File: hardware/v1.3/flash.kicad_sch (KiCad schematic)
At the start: 10 parts, among them U1 ECP5-CABGA256, U11 W25Q128JVS

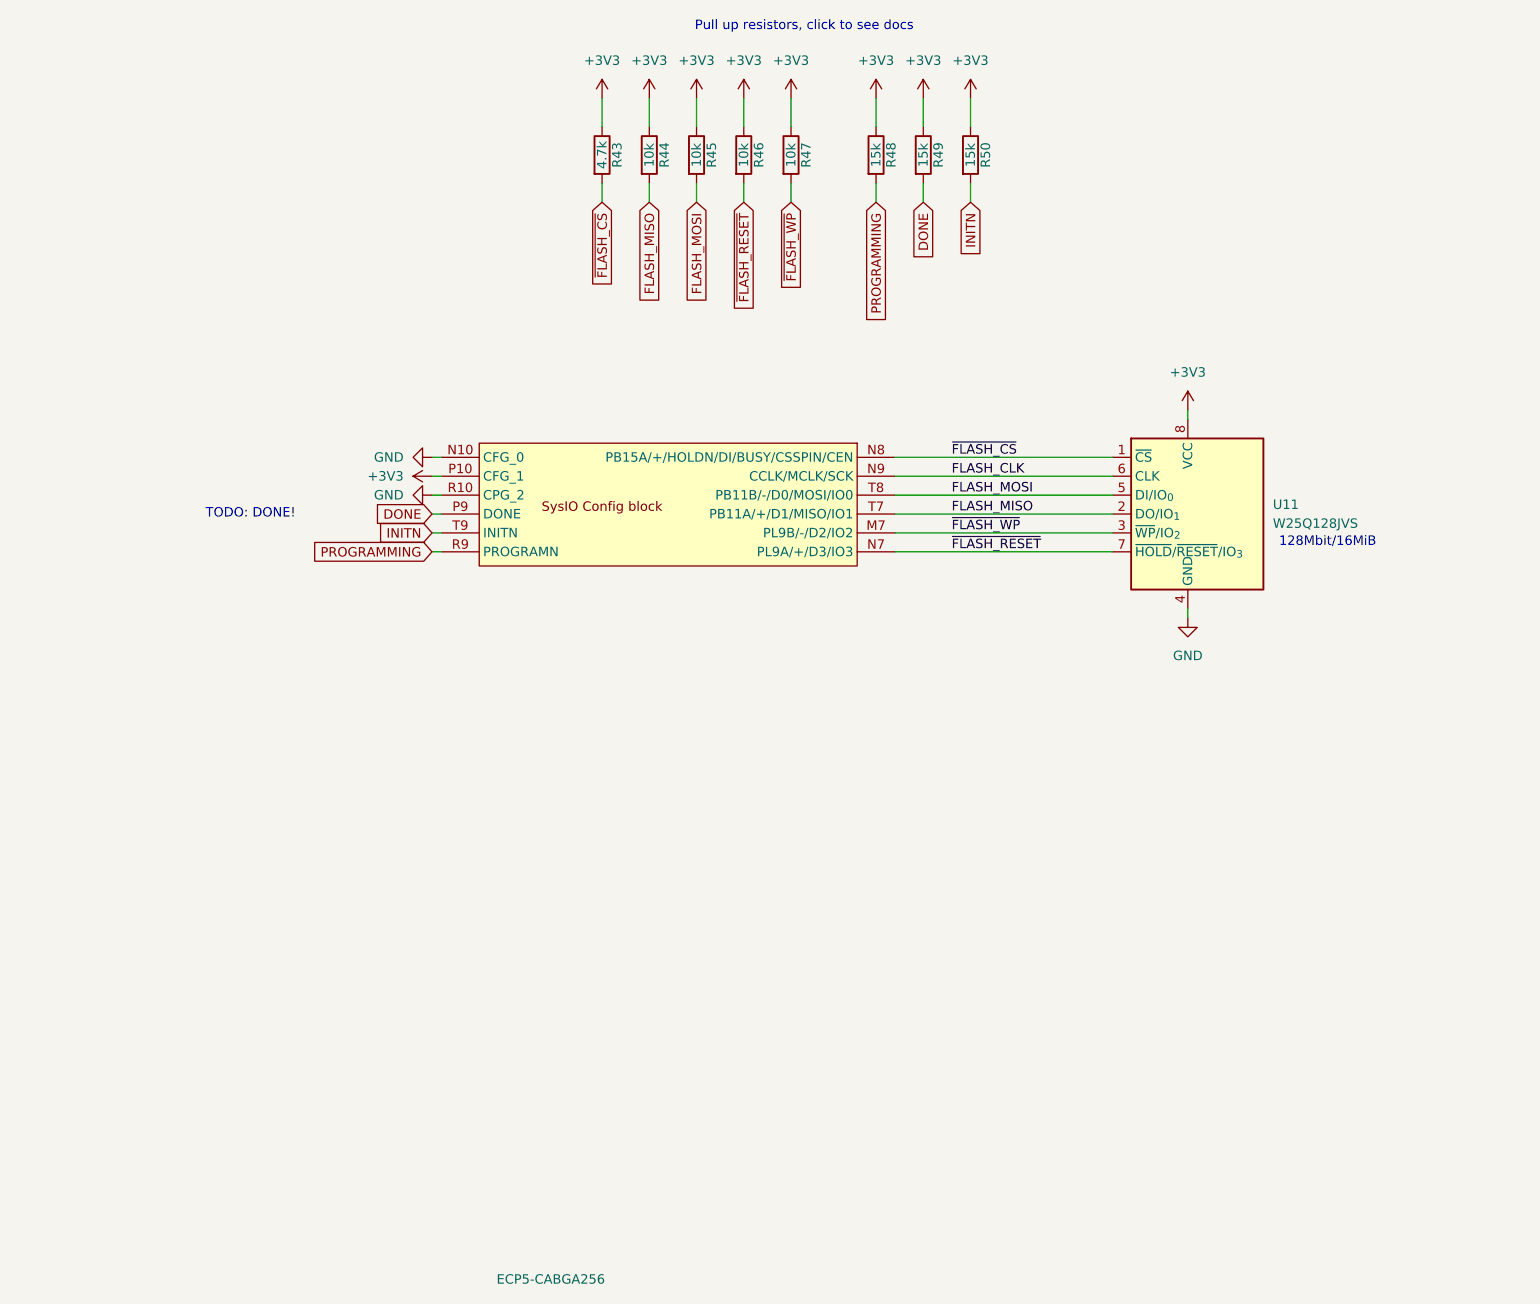
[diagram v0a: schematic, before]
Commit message: Refine README
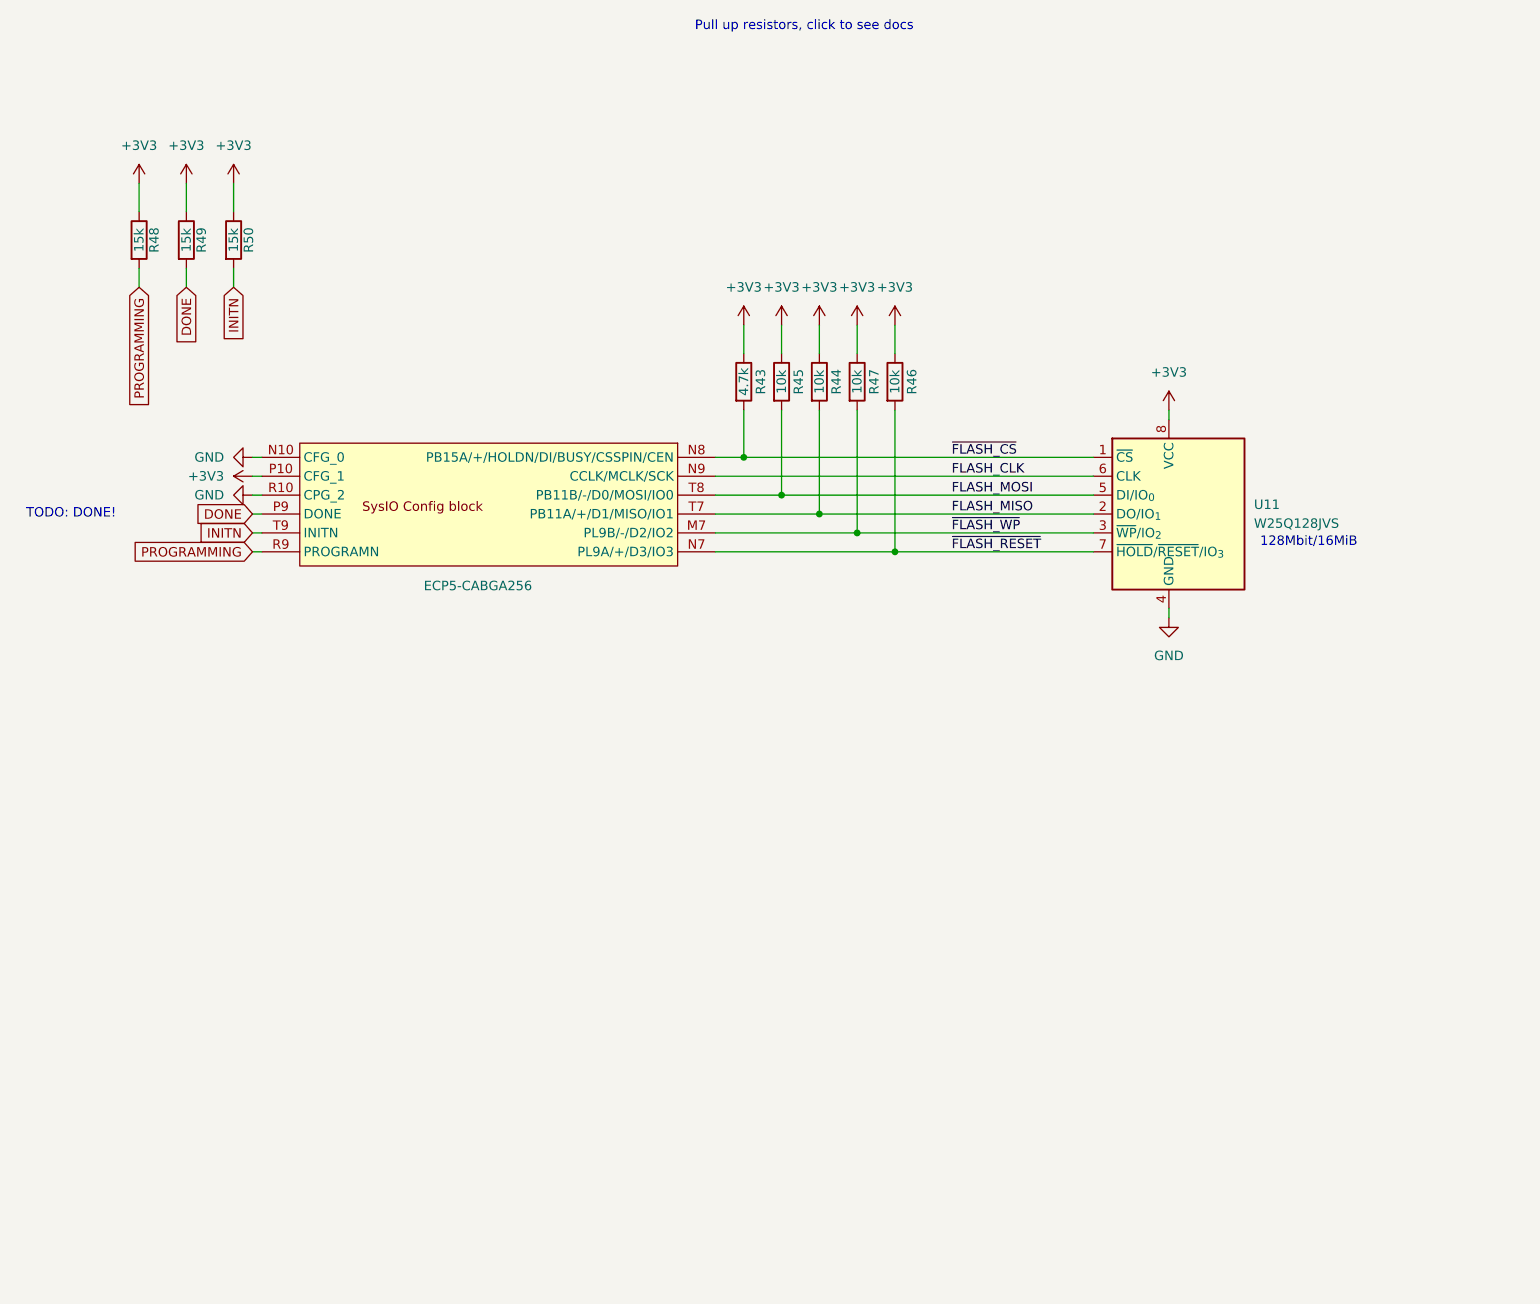
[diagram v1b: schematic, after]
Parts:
- R43: LCSC Link (none) -> https://lcsc.com/product-detail/Chip-Resistor-Surface-Mount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; LCSC Part # C25900 -> C25900; Manufactuer Part Number (none) -> 0402WGF4701TCE
- R44, R45, R46, R47: LCSC Link (none) -> https://lcsc.com/product-detail/Chip-Resistor-Surface-Mount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; Manufactuer Part Number (none) -> 0402WGF1002TCE
- R48, R49, R50: LCSC Link (none) -> https://lcsc.com/product-detail/Chip-Resistor-Surface-Mount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; Manufactuer Part Number (none) -> 0402WGF1502TCE
- U1: LCSC Link (none) -> https://lcsc.com/product-detail/Programmable-Logic-Device-C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; LCSC Part # (none) -> C1521614; Manufactuer Part Number (none) -> LFE5U-25F-6BG256C
- U11: LCSC Link (none) -> https://lcsc.com/product-detail/NOR-FLASH_Winbond-W25Q128JV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; Manufactuer Part Number (none) -> W25Q128JVSIQ
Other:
- moved on the sheet: R43, R44, R45, R46, R47, R48, R49, R50, U11

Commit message: Update files
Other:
- note added: "Pull up resistors from FPGA-TN-02039 CFG = 0b010 for MSPI mode"
- note removed: "Pull up resistors, click to see docs"
- note removed: "TODO: DONE!"
- moved on the sheet: R43, R44, R45, R46, R47, R48, R49, R50, U11

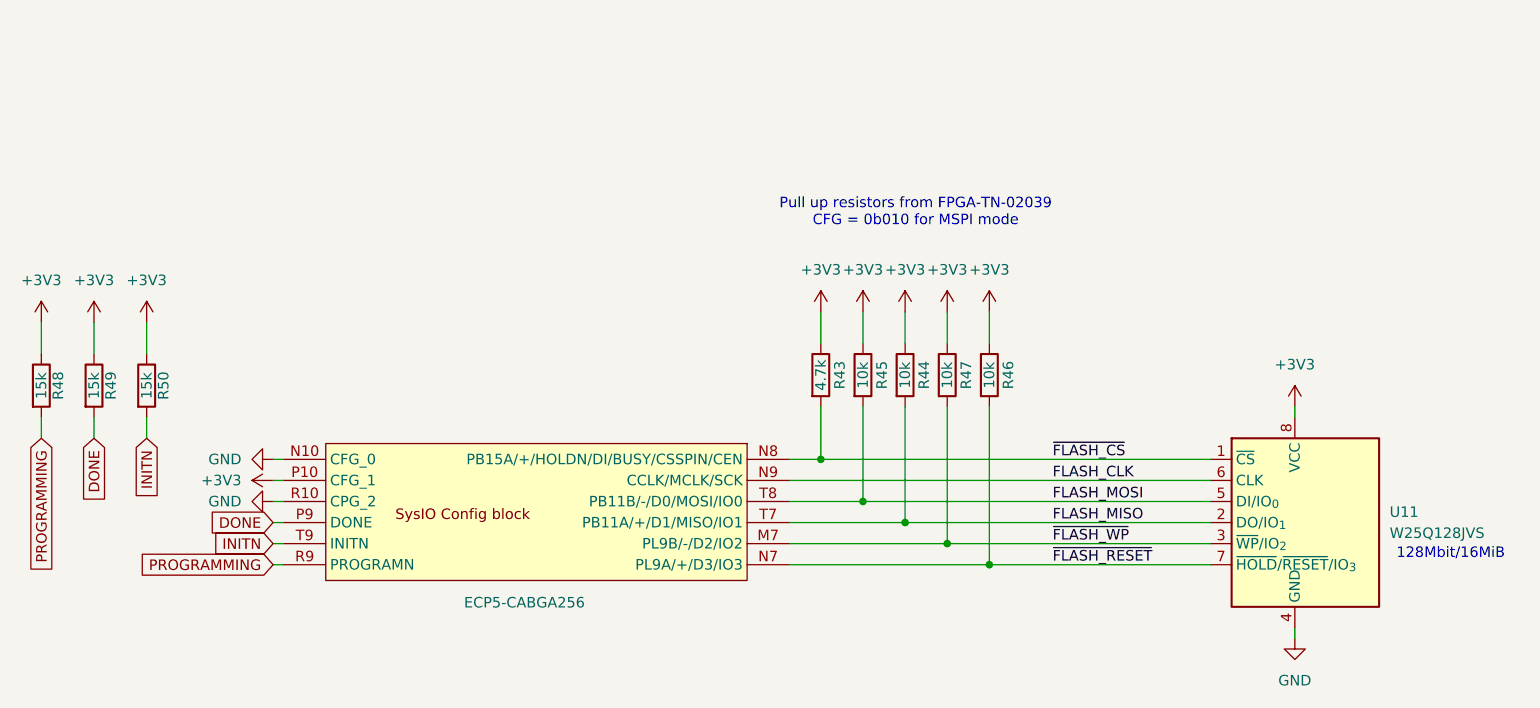
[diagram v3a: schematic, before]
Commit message: Improve makefile and hardware
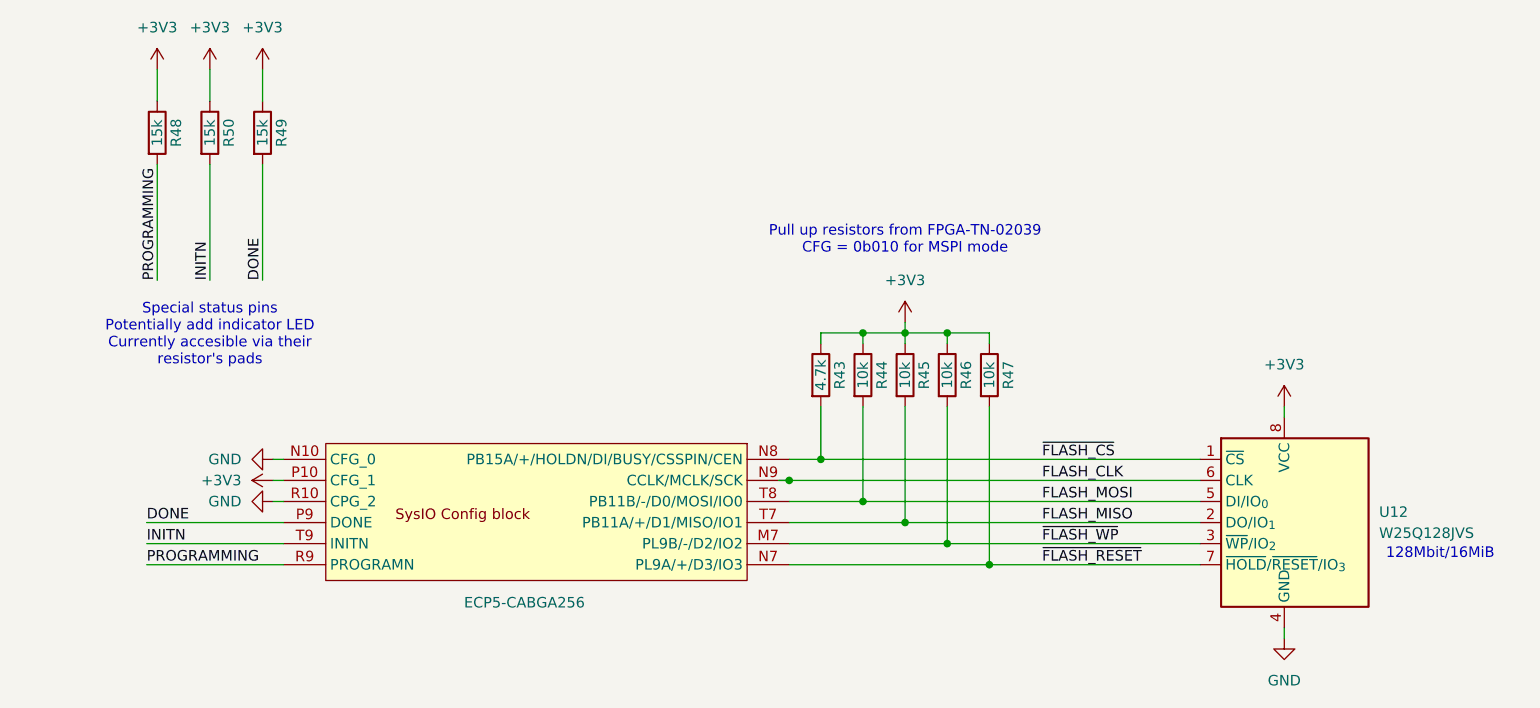
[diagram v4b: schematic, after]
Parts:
- renumbered R45 to R44, R44 to R45, R47 to R46, R46 to R47, U11 to U12
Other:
- note added: "Special status pins Potentially add indicator LED Currently accesible via their resistor's pads"
- title: Icepi zero -> Icepi Zero
- moved on the sheet: R48, R49, R50, U12
